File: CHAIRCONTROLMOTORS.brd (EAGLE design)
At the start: 35 x 49 mm, 39 parts, among them IC2 TCAN332DR, IC3 ATMEGA328P, IC4 MCP2515

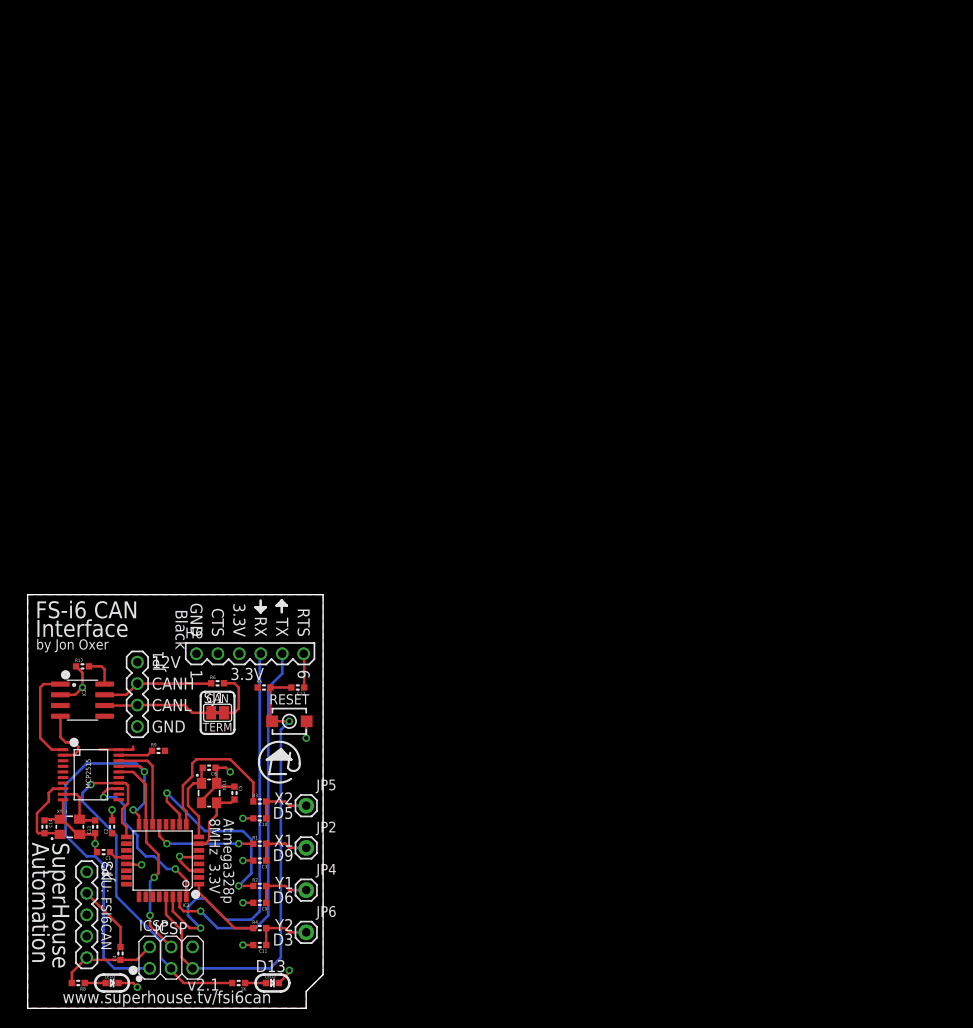
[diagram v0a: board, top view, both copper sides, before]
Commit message: Added XTxx external connections
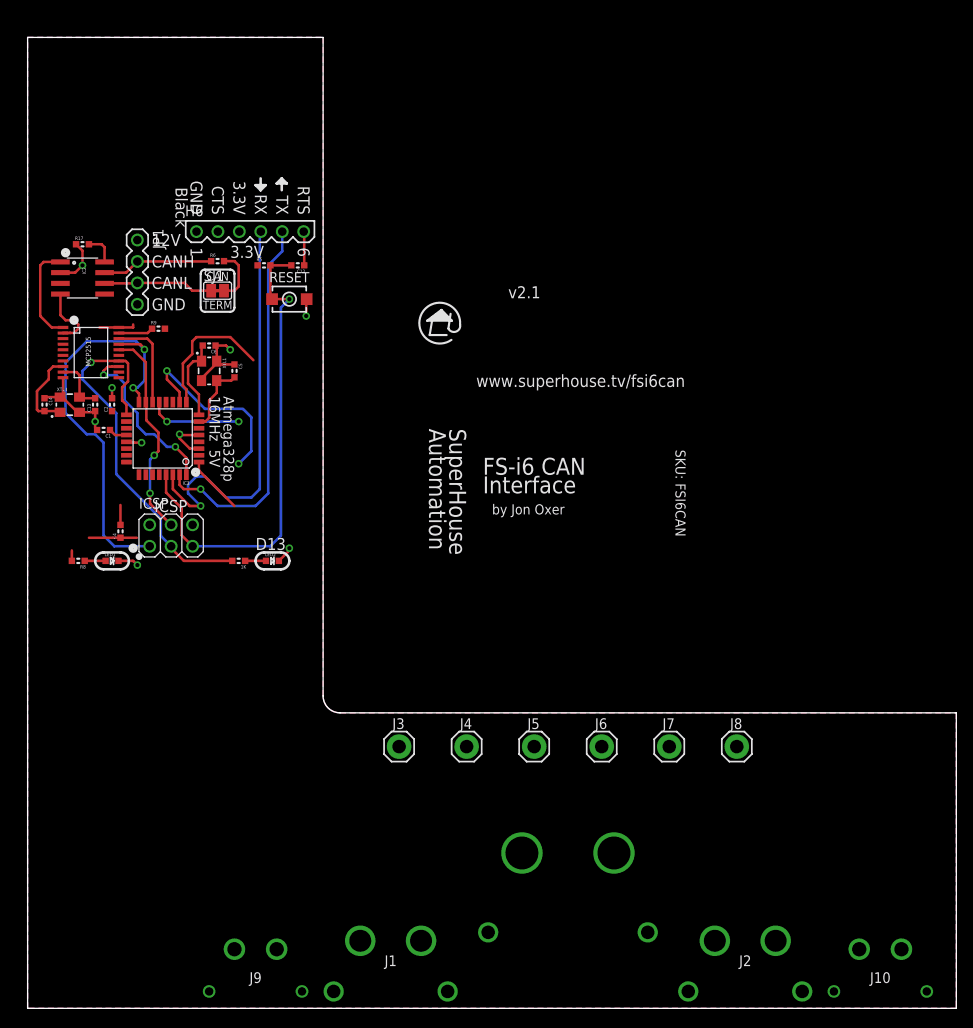
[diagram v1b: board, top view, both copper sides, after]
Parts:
- removed C10, C11, C3, C9: 1uF, SuperHouse-DiscreteSemi:C0603
- removed JP2, JP4, JP5, JP6: M01-PLAIN, SuperHouse-Connectors:1X01
- removed JP3: FS-i6, freetronics-jon:1X05
- removed R1, R2, R3, R4: 4K7, SuperHouse-DiscreteSemi:R0603
- added J1: LEFT MOTOR, SuperHouse-Connectors:XT60PW-F
- added J10, J9: XTXX-30F, SuperHouse-Connectors:XT30PW-F
- added J2: RIGHT MOTOR, SuperHouse-Connectors:XT60PW-F
- added J3, J4, J5, J6, J7, J8: M01-1.6MM, SuperHouse-Connectors:1X01-1.6MM
- added U$10: BATTERY, SuperHouse-Connectors:XT90PW-M
- IC2: value TCAN332DR -> MCP2551
- XTL1: value 8MHz -> 16MHz
- moved 1K 50.0 mm to (25.0, 53.0)
- moved C1 50.0 mm to (9.00, 68.5)
- moved C12 50.0 mm to (32.0, 88.0)
- moved C13 50.0 mm to (8.00, 71.5)
- moved C14 50.0 mm to (2.00, 71.5)
- moved C2 50.0 mm to (10.0, 71.5)
- moved C4 50.0 mm to (11.0, 56.5)
- moved C5 50.0 mm to (24.5, 75.5)
- moved C6 50.0 mm to (21.5, 78.5)
- moved H6 50.0 mm to (20.0, 92.0)
- moved IC2 50.0 mm to (6.50, 86.5)
- moved IC3 50.0 mm to (16.0, 67.5)
- moved IC4 50.0 mm to (7.50, 78.0)
- moved ICSP 50.0 mm to (17.0, 56.0)
- moved JP1 50.0 mm to (13.0, 91.0)
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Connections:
- net 12V renamed 24V
- removed net 3.3V: C2.1, C4.1, H6.3, IC2.3, IC3.18, IC3.4, IC3.6, IC4.20, ICSP.2, JP3.5, R5.1, R8.2, R9.2
- removed net FS_RESET: JP3.1
- removed net FS_SWD_CLK: JP3.4
- removed net FS_SWD_DIO: JP3.3
- removed net OUT_X1: C3.1, JP2.1, R1.2
- removed net OUT_X2: C10.1, JP5.1, R3.2
- removed net OUT_Y1: C9.1, JP4.1, R2.2
- removed net OUT_Y2: C11.1, JP6.1, R4.2
- new net 5V: C2.1, C4.1, H6.3, IC2.3, IC3.18, IC3.4, IC3.6, IC4.20, ICSP.2, R5.1, R8.2, R9.2
- new net N$10: J5.1, U$10.+
- new net N$13: J6.1, U$10.-
- new net N$14: J2.-, J7.1
- new net N$15: J2.+, J8.1
- new net N$3: J1.+, J4.1
- new net N$9: J1.-, J3.1
- net D3: no longer R4.1
- net D5: no longer R3.1
- net D6: no longer R2.1
- net D9: no longer R1.1
- net GND: no longer C10.2, C11.2, C3.2, C9.2, JP3.2
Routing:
- net 3.3V: track 16.3 -> 0.00 mm
- net 5V: track 0.00 -> 11.3 mm
- net GND: track 54.7 -> 44.1 mm, vias 13 -> 9
- net OUT_Y2: track 6.95 -> 0.00 mm
- net OUT_Y1: track 6.95 -> 0.00 mm
- net OUT_X2: track 6.95 -> 0.00 mm
- net OUT_X1: track 6.95 -> 0.00 mm
- net D5: track 18.7 -> 16.4 mm
- net D3: track 9.18 -> 6.94 mm
- net D9: track 12.9 -> 11.2 mm
- net D6: track 24.5 -> 22.7 mm
- added copper zone on layer 1, net 5V
- removed copper zone on layer 1, net 3.3V
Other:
- board size 35 x 49 mm -> 110 x 115 mm
- board text added: "Atmega328p 16MHz 5V"
- board text removed: "Atmega328p 8MHz 3.3V"
- board text removed: "X1 D9"
- board text removed: "X2 D5"
- board text removed: "Y1 D6"
- board text removed: "Y2 D3"

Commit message: Major schematic replacement to switch to 32U4 processor
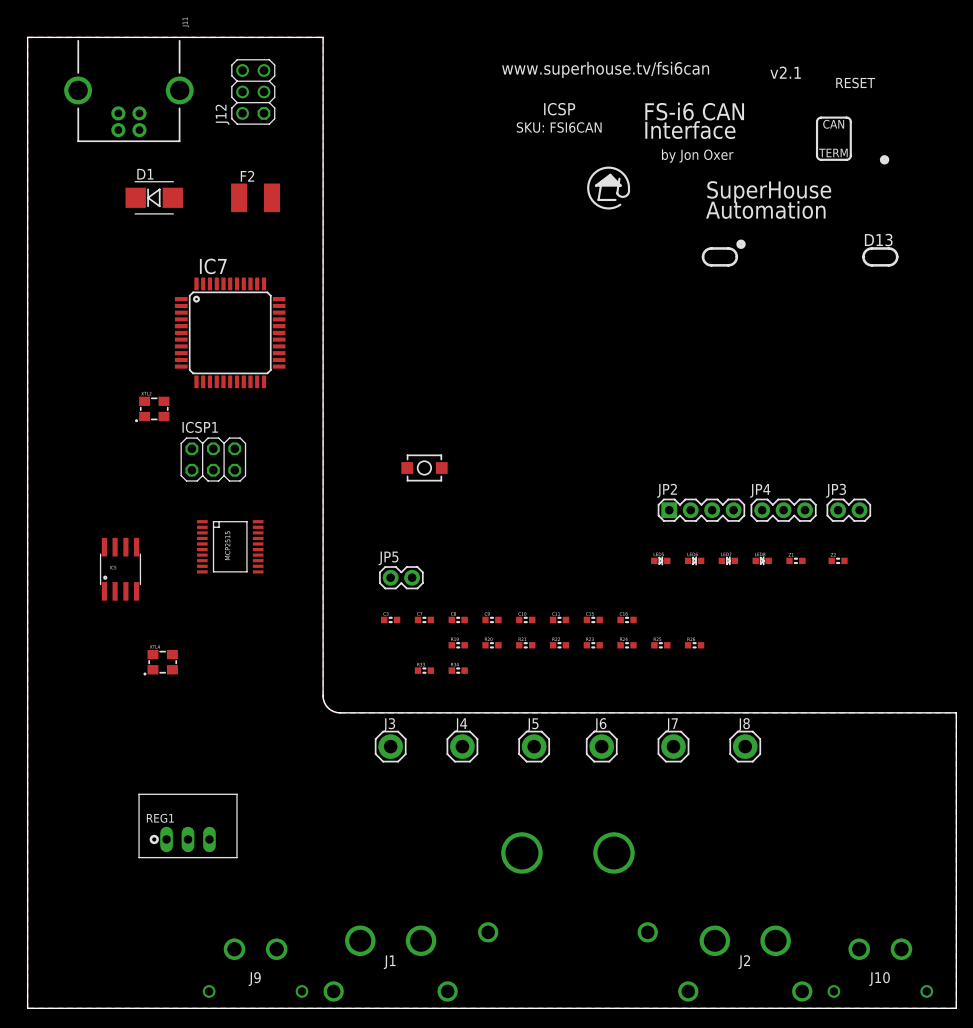
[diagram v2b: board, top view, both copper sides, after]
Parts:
- removed 1K: 1K, SuperHouse-DiscreteSemi:R0603
- removed C1, C12, C2: 100nF, SuperHouse-DiscreteSemi:C0603
- removed C13, C14, C5, C6: 15pF, SuperHouse-DiscreteSemi:C0603
- removed C4: 1uF, SuperHouse-DiscreteSemi:C0603
- removed H6: USB-TTL, SuperHouse-Connectors:1X06-P-RA
- removed IC2: MCP2551, SuperHouse-ICs:SO08
- removed IC3: ATMEGA328P, SuperHouse-MCUs:TQFP32-08
- removed IC4: MCP2515, SuperHouse-ICs:TSSOP20
- removed ICSP: ICSP, SuperHouse-Connectors:2X03-ICSP
- removed JP1: CAN, SuperHouse-Connectors:1X04-P
- removed LED1: BLUE, SuperHouse-LEDs:LED-0603
- removed LED2: RED, SuperHouse-LEDs:LED-0603
- removed R17, R5, R9: 10K, SuperHouse-DiscreteSemi:R0603
- removed R6: 120R, SuperHouse-DiscreteSemi:R0603
- removed R8: 4K7, SuperHouse-DiscreteSemi:R0603
- removed S21: RESET, SuperHouse-Switches:TACTILE_SMT_3X4X2
- removed SJ1: CAN Termination, SuperHouse-Jumpers:SJC
- removed XTL1, XTL3: 16MHz, SuperHouse-Oscillators:CRYSTAL-SMD-3X2
- added C10, C15, C16, C9: 15pF, freetronics-master-v1.1:0603
- added C11, C7: 1uF, freetronics-master-v1.1:0603
- added C3, C8: 100nF, freetronics-master-v1.1:0603
- added D1: 1N4004, freetronics-jon:SMB-DIODE
- added F2: 500mA PTC 1812, rcl:L1812
- added IC5: MCP2551, freetronics-original:SO08
- added IC6: MCP2515, MCP2515:TSSOP20
- added IC7: ATMEGA32U4NT, freetronics-jon:TQFP44
- added ICSP1: ICSP, pinhead:2X03
- added J11: USB-B-PTH, SuperHouse-Connectors:USB-B-PTH
- added J12: M02X3-PIN, SuperHouse-Connectors:2X03-P
- added JP2: CAN, freetronics-jon:1X04
- added JP3, JP5: PWR, freetronics-jon:1X02
- added JP4: PWR, freetronics-jon:1X03
- added LED5: RED, freetronics-jon:LED-0603
- added LED6, LED8: GREEN, freetronics-jon:LED-0603
- added LED7: BLUE, freetronics-jon:LED-0603
- added R19, R25, R26: 10K, freetronics-master-v1.1:0603
- added R20: 4K7, freetronics-jon:0603
- added R21, R22, R33: 1K, freetronics-jon:0603
- added R23, R24: 22R, freetronics-jon:0603
- added R34: 120R, freetronics-master-v1.1:0603
- added REG1: K7805-500R3, freetronics-jon:K78XX-500R3
- added S1: RESET, freetronics-jon:TACTILE_SWITCH_SMD_2PIN_TINY
- added XTL2, XTL4: 16MHz, freetronics-jon:CRYSTAL-SMD-3X2
- added Z1, Z2: PGB1010603, freetronics-master-v1.1:0603
- moved J3 1.00 mm to (43.0, 31.0)
- moved J8 1.00 mm to (85.0, 31.0)
- moved J4 0.50 mm to (51.5, 31.0)
- moved J7 0.50 mm to (76.5, 31.0)
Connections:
- removed net A6: IC3.19
- removed net A7: IC3.22
- removed net D0_RX: H6.4, IC3.30
- removed net D10_SS: IC3.14, IC4.18
- removed net D11_MOSI: IC3.15, IC4.16, ICSP.4
- removed net D12_MISO: IC3.16, IC4.17, ICSP.1
- removed net D13_SCK: 1K.2, IC3.17, IC4.14, ICSP.3
- removed net D1_TX: H6.5, IC3.31
- removed net D2: IC3.32, IC4.13
- removed net D3: IC3.1
- removed net D4: IC3.2
- removed net D6: IC3.10
- removed net D7: IC3.11
- removed net D8: IC3.12
- removed net D9: IC3.13
- removed net N$1: 1K.1, LED2.A
- removed net N$11: C5.2, IC3.7, XTL1.3
- removed net N$12: C6.2, IC3.8, XTL1.1
- removed net N$16: IC2.8, R17.2
- removed net N$17: IC4.19, R9.1
- removed net N$4: IC2.1, IC4.1
- removed net N$6: IC2.4, IC4.2
- removed net N$7: C13.2, IC4.9, XTL3.3
- removed net N$8: C14.2, IC4.8, XTL3.1
- removed net RTS: C12.1, H6.6
- new net 3V3: C11.2, IC7.6
- new net D+: J11.D+, R24.1, Z2.2
- new net D-: J11.D-, R23.1, Z1.2
- new net D0: IC7.20
- new net D1: IC7.21
- new net D10_A11: IC6.18, IC7.30
- new net D11: IC7.12
- new net D12: IC7.26
- new net D13: IC7.32, R33.1
- new net D2_SDA: IC6.13, IC7.19
- new net D3_SCL: IC7.18
- new net D4_A6: IC7.25
- new net D6_A8: IC7.27
- new net D7_AIN0: IC7.1
- new net D8_A9: IC7.28
- new net D9_A10: IC7.29
- new net HWB: IC7.33
- new net MISO: IC6.17, IC7.11, ICSP1.1
- new net MOSI: IC6.16, IC7.10, ICSP1.4
- new net N$28: C9.2, IC7.17, XTL2.3
- new net N$29: C10.2, IC7.16, XTL2.1
- new net N$30: LED7.A, R20.1
- new net N$31: LED5.A, R21.1
- new net N$32: LED6.A, R22.1
- new net N$33: IC6.19, R25.1
- new net N$34: IC5.1, IC6.1
- new net N$35: IC5.4, IC6.2
- new net N$36: IC5.8, R26.2
- new net N$37: C15.2, IC6.8, XTL4.3
- new net N$38: C16.2, IC6.9, XTL4.1
- new net N$39: JP2.1, JP3.2
- new net N$40: D1.C, F2.1
- new net N$43: LED8.A, R33.2
- new net N$44: JP5.2, R34.2
- new net RD+: IC7.4, R24.2
- new net RD-: IC7.3, R23.2
- new net RXLED_SS: IC7.8, LED6.C
- new net SCK: IC6.14, IC7.9, ICSP1.3
- new net TX_LED: IC7.22, LED5.C
- new net USB+: D1.A, J11.VBUS
- net 24V: now also JP3.1, JP4.2, REG1.1; no longer JP1.1
- net 5V: now also C3.1, C7.1, F2.2, IC5.3, IC6.20, IC7.14, IC7.2, IC7.24, IC7.34, IC7.44, IC7.7, ICSP1.2, R19.2, R20.2, R21.2, R22.2, R25.2, REG1.3; no longer C2.1, C4.1, H6.3, IC2.3, IC3.18, IC3.4, IC3.6, IC4.20, ICSP.2, R5.1, R8.2, R9.2
- net A0: now also IC7.36; no longer IC3.23
- net A1: now also IC7.37; no longer IC3.24
- net A2: now also IC7.38; no longer IC3.25
- net A3: now also IC7.39; no longer IC3.26
- net A4: now also IC7.40; no longer IC3.27
- net A5: now also IC7.41; no longer IC3.28
- net AREF: now also C8.1, IC7.42; no longer C1.1, IC3.20
- net CANH: now also IC5.7, JP2.2, JP5.1; no longer IC2.7, JP1.2, R6.1
- net CANL: now also IC5.6, JP2.3, R34.1; no longer IC2.6, JP1.3, SJ1.1
- net D5: now also IC7.31; no longer IC3.9
- net GND: now also C10.1, C11.1, C15.1, C16.1, C3.2, C7.2, C8.2, C9.1, IC5.2, IC6.10, IC7.15, IC7.23, IC7.35, IC7.43, IC7.5, ICSP1.6, J10.+, J11.GND, J11.SHLD1, J11.SHLD2, J9.+, JP2.4, JP4.1, LED7.C, LED8.C, R26.1, REG1.2, S1.1, XTL2.2, XTL2.4, XTL4.2, XTL4.4, Z1.1, Z2.1; no longer C1.2, C13.1, C14.1, C2.2, C4.2, C5.1, C6.1, H6.1, H6.2, IC2.2, IC3.21, IC3.3, IC3.5, IC4.10, ICSP.6, JP1.4, LED1.C, LED2.C, R17.1, S21.1, XTL1.2, XTL1.4, XTL3.2, XTL3.4
- net N$2: now also J9.-; no longer R6.2, SJ1.2
- net N$5: now also J10.-; no longer LED1.A, R8.1
- net RESET: now also IC7.13, ICSP1.5, R19.1, S1.2; no longer C12.2, IC3.29, ICSP.5, R5.2, S21.2
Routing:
- net RESET: track 57.8 -> 0.00 mm, vias 1 -> 0
- net D12_MISO: track 50.7 -> 0.00 mm, vias 2 -> 0
- net D0_RX: track 49.9 -> 0.00 mm, vias 1 -> 0
- net D13_SCK: track 45.8 -> 0.00 mm, vias 1 -> 0
- net D1_TX: track 45.1 -> 0.00 mm, vias 1 -> 0
- net GND: track 44.1 -> 0.00 mm, vias 9 -> 0
- net D11_MOSI: track 25.1 -> 0.00 mm, vias 2 -> 0
- net D6: track 22.7 -> 0.00 mm, vias 2 -> 0
- net D2: track 20.4 -> 0.00 mm, vias 2 -> 0
- net D5: track 16.4 -> 0.00 mm
- net CANH: track 13.2 -> 0.00 mm
- net CANL: track 13.0 -> 0.00 mm
- net N$4: track 11.8 -> 0.00 mm
- net 5V: track 11.3 -> 0.00 mm
- net D9: track 11.2 -> 0.00 mm, vias 2 -> 0
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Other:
- board text removed: "1"
- board text removed: "12V"
- board text removed: "3.3V"
- board text removed: "6"
- board text removed: "Atmega328p 16MHz 5V"
- board text removed: "Black"
- board text removed: "CANH"
- board text removed: "CANL"
- board text removed: "CTS"
- board text removed: "GND"
- board text removed: "RTS"
- board text removed: "RX"
- board text removed: "TX"

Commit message: Schematic cleanups and start of placement
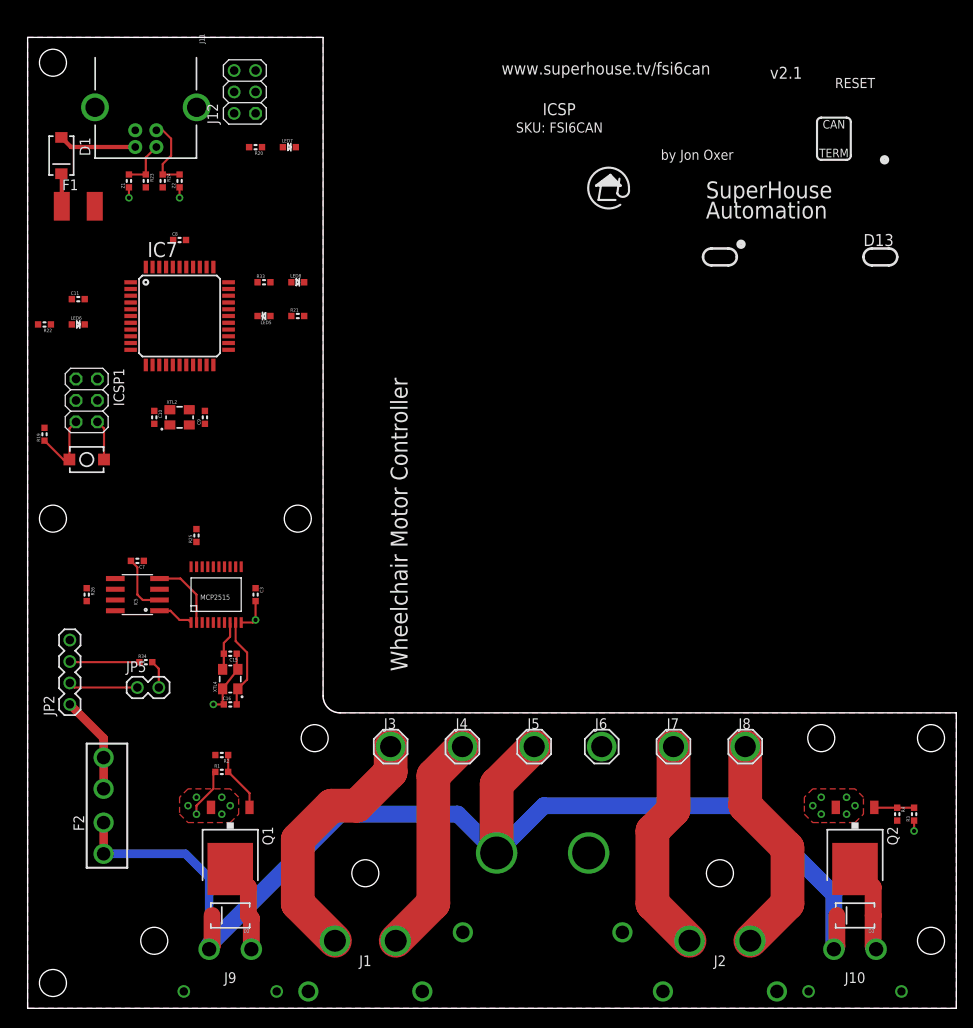
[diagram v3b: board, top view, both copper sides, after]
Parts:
- removed JP3: PWR, freetronics-jon:1X02
- removed JP4: PWR, freetronics-jon:1X03
- removed REG1: K7805-500R3, freetronics-jon:K78XX-500R3
- added D2, D3: (no value), SuperHouse-DiscreteSemi:SMA-DIODE
- added F1: 500mA PTC 1812, SuperHouse-Fuses:1812
- added Q1, Q2: NTD5867NLT4G, SuperHouse-DiscreteSemi:DPACK
- added R1, R3: 10K, SuperHouse-DiscreteSemi:R0603
- added R2, R4: 1K, SuperHouse-DiscreteSemi:R0603
- C10, C11, C15, C16, C3, C7, C8, C9: device freetronics-master-v1.1:0603 -> SuperHouse-DiscreteSemi:C0603
- D1: value 1N4004 -> SS56; device freetronics-jon:SMB-DIODE -> SuperHouse-DiscreteSemi:SMA-DIODE
- F2: value 500mA PTC 1812 -> 5A; device rcl:L1812 -> SuperHouse-Fuses:MCCQ-122
- IC5: device freetronics-original:SO08 -> SuperHouse-ICs:SO08
- IC6: device MCP2515:TSSOP20 -> SuperHouse-ICs:TSSOP20
- IC7: value ATMEGA32U4NT -> ATMEGA32U4NT-TQFP; device freetronics-jon:TQFP44 -> SuperHouse-MCUs:TQFP44
- J3, J4, J5, J6, J7, J8: value M01-1.6MM -> M01-2.5MM; device SuperHouse-Connectors:1X01-1.6MM -> SuperHouse-Connectors:1X01-2.5MM
- JP2: device freetronics-jon:1X04 -> SuperHouse-Connectors:1X04-P
- JP5: value PWR -> CAN TERM; device freetronics-jon:1X02 -> SuperHouse-Connectors:1X02-P
- LED5, LED6, LED7, LED8: device freetronics-jon:LED-0603 -> SuperHouse-LEDs:LED-0603
- R19, R25, R26, R34: device freetronics-master-v1.1:0603 -> SuperHouse-DiscreteSemi:R0603
- R20, R21, R22, R23, R24, R33: device freetronics-jon:0603 -> SuperHouse-DiscreteSemi:R0603
- S1: device freetronics-jon:TACTILE_SWITCH_SMD_2PIN_TINY -> SuperHouse-Switches:TACTILE_SMT_3X4X2
- XTL2, XTL4: device freetronics-jon:CRYSTAL-SMD-3X2 -> SuperHouse-Oscillators:CRYSTAL-SMD-3X2
- Z1, Z2: device freetronics-master-v1.1:0603 -> SuperHouse-DiscreteSemi:TVS0603
- moved Z1 90.9 mm to (12.0, 98.0), turned to 90 degrees
- moved Z2 90.0 mm to (18.0, 98.0), turned to 90 degrees
- moved LED6 78.2 mm to (6.00, 81.0)
- moved R24 77.8 mm to (16.0, 98.0), turned to 270 degrees
- moved R23 76.4 mm to (14.0, 98.0), turned to 270 degrees
- moved JP2 74.6 mm to (5.00, 36.0), turned to 90 degrees
- moved F2 74.2 mm to (9.00, 24.0), turned to 90 degrees
- moved R26 72.2 mm to (7.00, 49.0), turned to 270 degrees
- moved R22 71.9 mm to (2.00, 81.0), turned to 180 degrees
- moved LED7 71.4 mm to (31.0, 102.0)
- moved C11 68.5 mm to (6.00, 84.0)
- moved R20 65.3 mm to (27.0, 102.0), turned to 180 degrees
- moved LED8 64.1 mm to (32.0, 86.0)
- moved R25 56.5 mm to (20.0, 56.0), turned to 90 degrees
- moved C8 55.8 mm to (18.0, 91.0)
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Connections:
- removed net N$10: J5.1, U$10.+
- removed net N$13: J6.1, U$10.-
- removed net N$39: JP2.1, JP3.2
- removed net N$5: J10.-
- new net LEFT_BRAKE: D2.A, J9.-, Q1.2
- new net LEFT_BRAKE_CONTROL: R2.2
- new net N$1: Q1.1, R1.2, R2.1
- new net N$4: Q2.1, R3.2, R4.1
- new net N$7: J12.2
- new net N$8: J12.1
- new net RIGHT_BRAKE: D3.A, J10.-, Q2.2
- new net RIGHT_BRAKE_CONTROL: R4.2
- net 24V: now also D2.C, D3.C, F2.1, F2.2, J10.+, J5.1, J9.+, U$10.+; no longer JP3.1, JP4.2, REG1.1
- net 5V: now also F1.2, J12.3, J12.4; no longer F2.2, ICSP1.2, REG1.3
- net GND: now also J12.5, J12.6, J6.1, Q1.3, Q2.3, R1.1, R3.1, U$10.-; no longer J10.+, J9.+, JP4.1, REG1.2
- net N$2: now also F2.3, F2.4, JP2.1; no longer J9.-
- net N$40: now also F1.1; no longer F2.1
- net USB+: now also ICSP1.2
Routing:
- net 24V: track 0.00 -> 144.1 mm
- net GND: track 0.00 -> 33.8 mm, vias 0 -> 17
- net N$9: track 0.00 -> 31.1 mm
- net N$15: track 0.00 -> 26.9 mm
- net N$3: track 0.00 -> 26.3 mm
- net N$14: track 0.00 -> 25.9 mm
- net N$2: track 0.00 -> 11.7 mm
- net N$38: track 0.00 -> 10.8 mm
- net RIGHT_BRAKE: track 0.00 -> 10.5 mm
- net LEFT_BRAKE: track 0.00 -> 10.5 mm
- net USB+: track 0.00 -> 9.22 mm
- net D+: track 0.00 -> 8.82 mm
- net RESET: track 0.00 -> 8.66 mm
- net N$35: track 0.00 -> 8.48 mm
- net CANL: track 0.00 -> 8.27 mm
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- added copper zone on layer 1, net GND
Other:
- board text added: "Wheelchair Motor Controller"
- board text removed: "FS-i6 CAN Interface"

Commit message: More routing
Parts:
- J12: value M02X3-PIN -> RoboClaw
- moved R21 12.5 mm to (26.0, 71.0), turned to 180 degrees
- moved LED5 9.22 mm to (26.0, 73.0)
- moved Z1 6.00 mm to (18.0, 98.0)
- moved Z2 6.00 mm to (12.0, 98.0)
- moved J12 5.39 mm to (25.0, 111.0), turned to 270 degrees
- moved C9 5.00 mm to (18.0, 66.0), turned to 0 degrees
- moved C10 3.61 mm to (18.0, 72.0), turned to 180 degrees
- moved C8 3.16 mm to (15.0, 92.0), turned to 180 degrees
- moved R33 3.00 mm to (31.0, 86.0)
- moved LED8 2.24 mm to (31.0, 88.0), turned to 180 degrees
- moved R23 2.00 mm to (16.0, 98.0)
- moved R24 2.00 mm to (14.0, 98.0)
- moved XTL2 1.00 mm to (18.0, 69.0), turned to 270 degrees
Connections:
- removed net N$7: J12.2
- removed net N$8: J12.1
- net D8_A9: now also J12.1
- net D9_A10: now also J12.2
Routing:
- net MISO: track 0.00 -> 47.5 mm, vias 0 -> 2
- net D10_A11: track 0.00 -> 46.8 mm
- net SCK: track 0.00 -> 46.7 mm, vias 0 -> 1
- net MOSI: track 0.00 -> 38.7 mm
- net USB+: track 9.22 -> 40.4 mm
- net GND: track 33.8 -> 62.0 mm, vias 17 -> 24
- net D2_SDA: track 0.00 -> 25.7 mm
- net RD+: track 0.00 -> 16.7 mm
- net RESET: track 8.66 -> 24.9 mm, vias 0 -> 1
- net RD-: track 0.00 -> 15.9 mm
- net CANH: track 8.22 -> 20.4 mm, vias 0 -> 1
- net N$28: track 0.00 -> 12.1 mm
- net CANL: track 8.27 -> 18.7 mm
- net N$29: track 0.00 -> 6.12 mm
- net AREF: track 0.00 -> 4.46 mm
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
